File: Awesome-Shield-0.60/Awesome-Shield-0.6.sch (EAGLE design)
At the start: 21 parts, among them J1 PORT1, J2 PORT2, J3 PORT3, SW1 SPST_TACT-EVQQ2, SW2 DPDT, U1 LIGHTSENSORTEMT6000

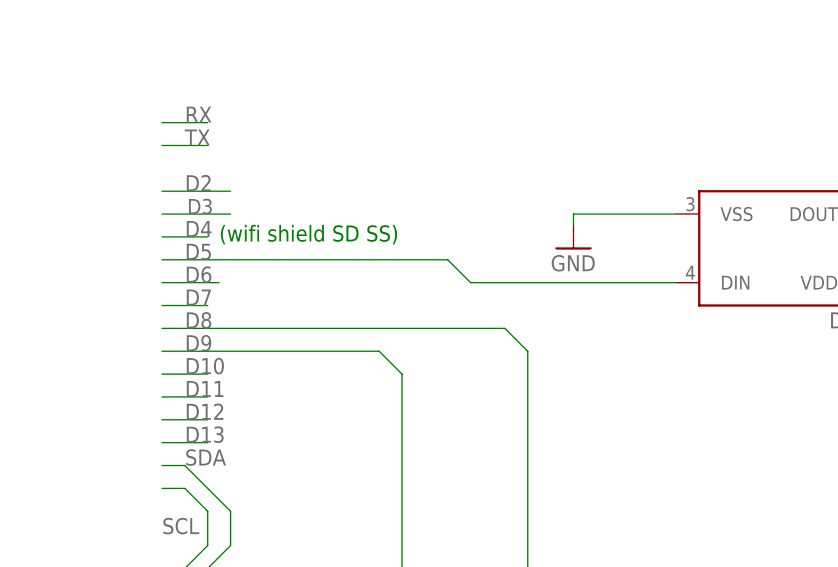
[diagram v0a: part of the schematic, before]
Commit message: added 330R resistor to LED data line
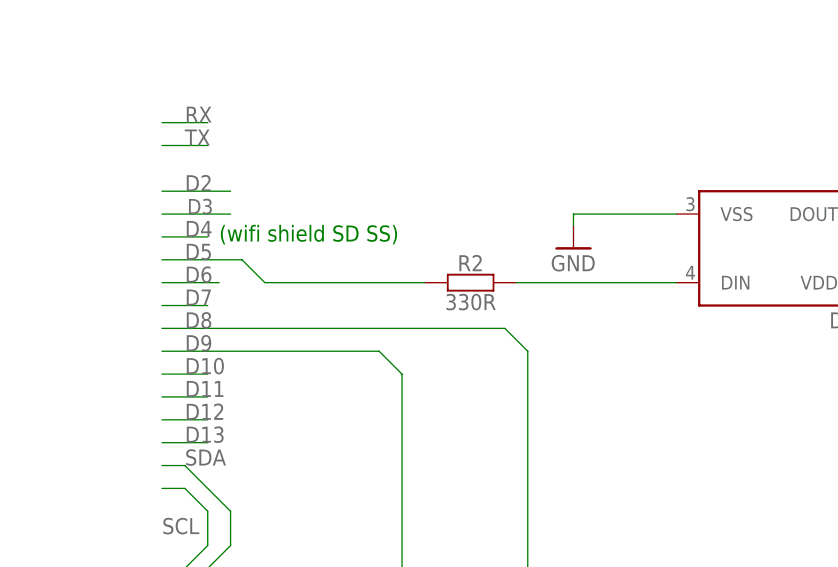
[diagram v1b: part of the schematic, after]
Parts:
- added R2: 330R, we-rcl:RESISTOR-1206
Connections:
- new net N$3: D1.DIN, R2.2
- net D5: now also R2.1; no longer D1.DIN
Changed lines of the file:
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@@
 <?xml version="1.0" encoding="utf-8"?>
 <!DOCTYPE eagle SYSTEM "eagle.dtd">
-<eagle version="7.6.0">
+<eagle version="7.2.0">
 <drawing>
 <settings>
@@
 <setting verticaltext="up"/>
 </settings>
-<grid distance="0.1" unitdist="inch" unit="inch" style="lines" multiple="1" display="no" altdistance="0.01" altunitdist="inch" altunit="inch"/>
+<grid distance="0.1" unitdist="inch" unit="inch" style="lines" multiple="1" display="yes" altdistance="0.01" altunitdist="inch" altunit="inch"/>
 <layers>
 <layer number="1" name="Top" color="4" fill="1" visible="no" active="no"/>
@@
 <part name="R1" library="rcl" deviceset="R-EU_" device="R1206" value="TBD"/>
 <part name="U$1" library="buzzer-loudity-bzel-t68-0808" deviceset="LOUDITY-BZEL-T68" device="0808"/>
+<part name="R2" library="we-rcl" deviceset="RESISTOR" device="-1206" value="330R"/>
 </parts>
 <sheets>
@@
 <instance part="R1" gate="G$1" x="220.98" y="135.89" rot="R90"/>
 <instance part="U$1" gate="G$1" x="218.44" y="111.76" rot="R270"/>
+<instance part="R2" gate="R" x="228.6" y="180.34"/>
 </instances>
 <busses>
@@
 <segment>
 <label x="196.85" y="182.88" size="1.778" layer="95"/>
-<pinref part="D1" gate="G$1" pin="DIN"/>
-<wire x1="251.46" y1="180.34" x2="228.6" y2="180.34" width="0.1524" layer="91"/>
-<wire x1="194.31" y1="182.88" x2="226.06" y2="182.88" width="0.1524" layer="91"/>
-<wire x1="226.06" y1="182.88" x2="228.6" y2="180.34" width="0.1524" layer="91"/>
+<wire x1="194.31" y1="182.88" x2="203.2" y2="182.88" width="0.1524" layer="91"/>
+<wire x1="203.2" y1="182.88" x2="205.74" y2="180.34" width="0.1524" layer="91"/>
+<pinref part="R2" gate="R" pin="1"/>
+<wire x1="205.74" y1="180.34" x2="223.52" y2="180.34" width="0.1524" layer="91"/>
 </segment>
 <segment>
@@
 </segment>
 </net>
+<net name="N$3" class="0">
+<segment>
+<pinref part="R2" gate="R" pin="2"/>
+<pinref part="D1" gate="G$1" pin="DIN"/>
+<wire x1="233.68" y1="180.34" x2="251.46" y2="180.34" width="0.1524" layer="91"/>
+</segment>
+</net>

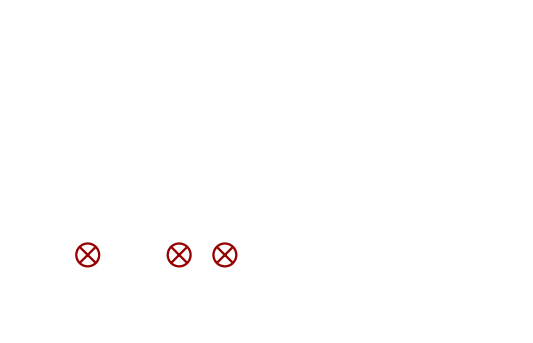
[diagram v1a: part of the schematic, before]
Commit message: changed fiducials to Watterott standard 0.7mm
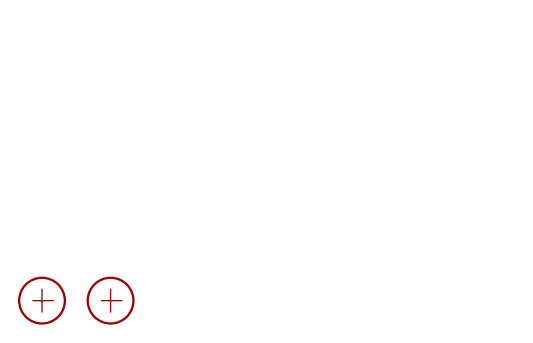
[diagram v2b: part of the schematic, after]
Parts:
- removed FID1, FID3, FID4: FIDUCIAL1X2, SparkFun-Aesthetics:FIDUCIAL1X2
- added X1, X2: PASSER-07, we-symbol:PASSER-07
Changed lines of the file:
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@@
 <part name="J1" library="Seeed-OPL-Connector" deviceset="GROVE-CONNECTOR-SMD(4+2P-2.0)" device="" value="PORT1"/>
 <part name="J2" library="Seeed-OPL-Connector" deviceset="GROVE-CONNECTOR-SMD(4+2P-2.0)" device="" value="PORT2"/>
-<part name="FID1" library="SparkFun-Aesthetics" deviceset="FIDUCIAL" device="1X2"/>
-<part name="FID3" library="SparkFun-Aesthetics" deviceset="FIDUCIAL" device="1X2"/>
-<part name="FID4" library="SparkFun-Aesthetics" deviceset="FIDUCIAL" device="1X2"/>
 <part name="U1" library="SparkFun-Sensors" deviceset="LIGHTSENSOR" device="TEMT6000"/>
 <part name="JP4" library="adafruit" deviceset="PINHD-1X10" device=""/>
@@
 <part name="U$1" library="buzzer-loudity-bzel-t68-0808" deviceset="LOUDITY-BZEL-T68" device="0808"/>
 <part name="R2" library="we-rcl" deviceset="RESISTOR" device="-1206" value="330R"/>
+<part name="X1" library="we-symbol" deviceset="PASSER" device="-07"/>
+<part name="X2" library="we-symbol" deviceset="PASSER" device="-07"/>
 </parts>
 <sheets>
@@
 <instance part="J1" gate="G$1" x="166.37" y="105.41"/>
 <instance part="J2" gate="G$1" x="325.12" y="105.41"/>
-<instance part="FID1" gate="G$1" x="15.24" y="15.24"/>
-<instance part="FID3" gate="G$1" x="25.4" y="15.24"/>
-<instance part="FID4" gate="G$1" x="30.48" y="15.24"/>
 <instance part="U1" gate="G$1" x="77.47" y="116.84"/>
 <instance part="JP4" gate="G$1" x="59.08" y="202.1"/>
@@
 <instance part="U$1" gate="G$1" x="218.44" y="111.76" rot="R270"/>
 <instance part="R2" gate="R" x="228.6" y="180.34"/>
+<instance part="X1" gate="X" x="10.16" y="10.16"/>
+<instance part="X2" gate="X" x="17.78" y="10.16"/>
 </instances>
 <busses>
